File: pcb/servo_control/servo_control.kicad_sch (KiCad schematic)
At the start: 49 parts, among them J1 USB_B_Micro, J10 Conn_01x03_Female, J11 Conn_01x03_Female, J12 Conn_01x03_Female, J13 Conn_01x03_Female, J14 Conn_01x03_Female, J15 Conn_01x03_Female, J16 Conn_01x03_Female, J17 Conn_01x03_Female, J18 Conn_01x03_Female, J19 Conn_01x03_Female, J20 Conn_01x03_Female, J21 Conn_01x06_Male, J3 Conn_01x03_Female, J4 Conn_01x03_Female, J5 Conn_01x03_Female, J6 Conn_01x03_Female, J7 Conn_01x03_Female, J8 Conn_01x03_Female, J9 Conn_01x03_Female, SW1 ESP_PROG, SW2 ESP_RST, U1 PCA9685BS, U2 LM317_SOT-223, U3 ESP32-WROOM-32, U4 MPU-9250, U5 PCA9685BS

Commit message: finish pcb
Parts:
- removed D3: LED, LED_SMD:LED_0603_1608Metric, symbol Device:LED
- removed R5: 1K, Resistor_SMD:R_0603_1608Metric, symbol Device:R
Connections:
- net LED_1: now also U3.9 (IO33)
- net LED_2: now also U3.8 (IO32)
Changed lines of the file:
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@@
-    (stroke (width 0) (type default) (color 0 0 0 0))
-  )
-  (wire (pts (xy 284.48 45.72) (xy 289.56 45.72))
     (stroke (width 0) (type default) (color 0 0 0 0))
   )
@@
     (stroke (width 0) (type default) (color 0 0 0 0))
   )
-  (wire (pts (xy 297.18 45.72) (xy 302.26 45.72))
-    (stroke (width 0) (type default) (color 0 0 0 0))
-  )
   (wire (pts (xy 147.32 215.9) (xy 152.4 215.9))
     (stroke (width 0) (type default) (color 0 0 0 0))
@@
     (stroke (width 0) (type default) (color 0 0 0 0))
   )
-  (wire (pts (xy 309.88 45.72) (xy 317.5 45.72))
-    (stroke (width 0) (type default) (color 0 0 0 0))
-  )
   (polyline (pts (xy 15.24 278.13) (xy 120.65 278.13))
     (stroke (width 0) (type default) (color 0 0 0 0))
@@
     (stroke (width 0) (type default) (color 0 0 0 0))
   )
+  (wire (pts (xy 80.01 250.19) (xy 83.82 250.19))
+    (stroke (width 0) (type default) (color 0 0 0 0))
+  )
   (wire (pts (xy 165.1 215.9) (xy 170.18 215.9))
     (stroke (width 0) (type default) (color 0 0 0 0))
@@
     (stroke (width 0) (type default) (color 0 0 0 0))
   )
+  (wire (pts (xy 83.82 248.92) (xy 85.09 248.92))
+    (stroke (width 0) (type default) (color 0 0 0 0))
+  )
   (wire (pts (xy 373.38 91.44) (xy 377.19 91.44))
     (stroke (width 0) (type default) (color 0 0 0 0))
   )
-  (polyline (pts (xy 269.24 15.24) (xy 269.24 49.53))
+  (polyline (pts (xy 269.24 15.24) (xy 269.24 39.37))
     (stroke (width 0) (type default) (color 0 0 0 0))
   )
@@
     (stroke (width 0) (type default) (color 0 0 0 0))
   )
+  (wire (pts (xy 83.82 250.19) (xy 83.82 248.92))
+    (stroke (width 0) (type default) (color 0 0 0 0))
+  )
   (polyline (pts (xy 358.14 190.5) (xy 358.14 158.75))
     (stroke (width 0) (type default) (color 0 0 0 0))
@@
     (stroke (width 0) (type default) (color 0 0 0 0))
   )
+  (wire (pts (xy 80.01 252.73) (xy 85.09 252.73))
+    (stroke (width 0) (type default) (color 0 0 0 0))
+  )
   (polyline (pts (xy 90.17 113.03) (xy 90.17 71.12))
     (stroke (width 0) (type default) (color 0 0 0 0))
@@
     (stroke (width 0) (type default) (color 0 0 0 0))
   )
-  (polyline (pts (xy 326.39 49.53) (xy 326.39 15.24))
+  (polyline (pts (xy 326.39 39.37) (xy 326.39 15.24))
     (stroke (width 0) (type default) (color 0 0 0 0))
   )
@@
     (stroke (width 0) (type default) (color 0 0 0 0))
   )
-  (polyline (pts (xy 269.24 49.53) (xy 326.39 49.53))
+  (polyline (pts (xy 269.24 39.37) (xy 326.39 39.37))
     (stroke (width 0) (type default) (color 0 0 0 0))
   )
@@
     )
   )
+  (global_label "LED_2" (shape input) (at 85.09 248.92 0) (fields_autoplaced)
+    (effects (font (size 1.27 1.27)) (justify left))
+    (property "Intersheet References" "${INTERSHEET_REFS}" (id 0) (at 93.1274 248.8406 0)
+      (effects (font (size 1.27 1.27)) (justify left) hide)
+    )
+  )
   (global_label "VCC" (shape input) (at 370.84 207.01 180) (fields_autoplaced)
     (effects (font (size 1.27 1.27)) (justify right))
@@
     )
   )
-  (global_label "GND" (shape input) (at 317.5 45.72 0) (fields_autoplaced)
-    (effects (font (size 1.27 1.27)) (justify left))
-    (property "Intersheet References" "${INTERSHEET_REFS}" (id 0) (at 323.7836 45.6406 0)
-      (effects (font (size 1.27 1.27)) (justify left) hide)
-    )
-  )
   (global_label "PWM_0_13" (shape input) (at 370.84 179.07 180) (fields_autoplaced)
     (effects (font (size 1.27 1.27)) (justify right))
@@
     )
   )
+  (global_label "LED_1" (shape input) (at 85.09 252.73 0) (fields_autoplaced)
+    (effects (font (size 1.27 1.27)) (justify left))
+    (property "Intersheet References" "${INTERSHEET_REFS}" (id 0) (at 93.1274 252.6506 0)
+      (effects (font (size 1.27 1.27)) (justify left) hide)
+    )
+  )
   (global_label "FTDI_CTS" (shape input) (at 73.66 54.61 0) (fields_autoplaced)
     (effects (font (size 1.27 1.27)) (justify left))
@@
     (property "Intersheet References" "${INTERSHEET_REFS}" (id 0) (at 160.7398 65.9606 0)
       (effects (font (size 1.27 1.27)) (justify left) hide)
-    )
-  )
-  (global_label "LED_3" (shape input) (at 284.48 45.72 180) (fields_autoplaced)
-    (effects (font (size 1.27 1.27)) (justify right))
-    (property "Intersheet References" "${INTERSHEET_REFS}" (id 0) (at 276.4426 45.6406 0)
-      (effects (font (size 1.27 1.27)) (justify right) hide)
     )
   )
@@
     )
     (property "Datasheet" "~" (id 3) (at 27.94 204.47 0)
-      (effects (font (size 1.27 1.27)) hide)
-    )
-    (pin "1")
-    (pin "2")
-  )
-  (symbol (lib_id "Device:R") (at 293.37 45.72 90) (unit 1)
-    (in_bom yes) (on_board yes) (fields_autoplaced)
-    (property "Reference" "R5" (id 0) (at 293.37 39.37 90))
-    (property "Value" "1K" (id 1) (at 293.37 41.91 90))
-    (property "Footprint" "Resistor_SMD:R_0603_1608Metric" (id 2) (at 293.37 47.498 90)
-      (effects (font (size 1.27 1.27)) hide)
-    )
-    (property "Datasheet" "~" (id 3) (at 293.37 45.72 0)
-      (effects (font (size 1.27 1.27)) hide)
-    )
-    (pin "1")
-    (pin "2")
-  )
-  (symbol (lib_id "Device:LED") (at 306.07 45.72 180) (unit 1)
-    (in_bom yes) (on_board yes)
-    (property "Reference" "D3" (id 0) (at 306.07 41.91 0))
-    (property "Value" "LED" (id 1) (at 306.07 39.37 0))
-    (property "Footprint" "LED_SMD:LED_0603_1608Metric" (id 2) (at 306.07 45.72 0)
-      (effects (font (size 1.27 1.27)) hide)
-    )
-    (property "Datasheet" "~" (id 3) (at 306.07 45.72 0)
       (effects (font (size 1.27 1.27)) hide)
     )
@@
       (reference "D2") (unit 1) (value "LED") (footprint "LED_SMD:LED_0603_1608Metric")
     )
-    (path "/0e3cf2b7-1e28-4d8a-863a-31ad64beb94b"
-      (reference "D3") (unit 1) (value "LED") (footprint "LED_SMD:LED_0603_1608Metric")
-    )
     (path "/9c8a2cf4-c30a-426a-b3e9-2e2ded2f331a"
       (reference "J1") (unit 1) (value "USB_B_Micro") (footprint "Connector_USB:USB_Micro-B_Molex-105017-0001")
@@
       (reference "R4") (unit 1) (value "1K") (footprint "Resistor_SMD:R_0603_1608Metric")
     )
-    (path "/0e2c80ab-b30b-4b41-93fc-dc4b3b81fc4c"
-      (reference "R5") (unit 1) (value "1K") (footprint "Resistor_SMD:R_0603_1608Metric")
-    )
     (path "/6f2988a4-b516-472d-b2a2-6928c828e26c"

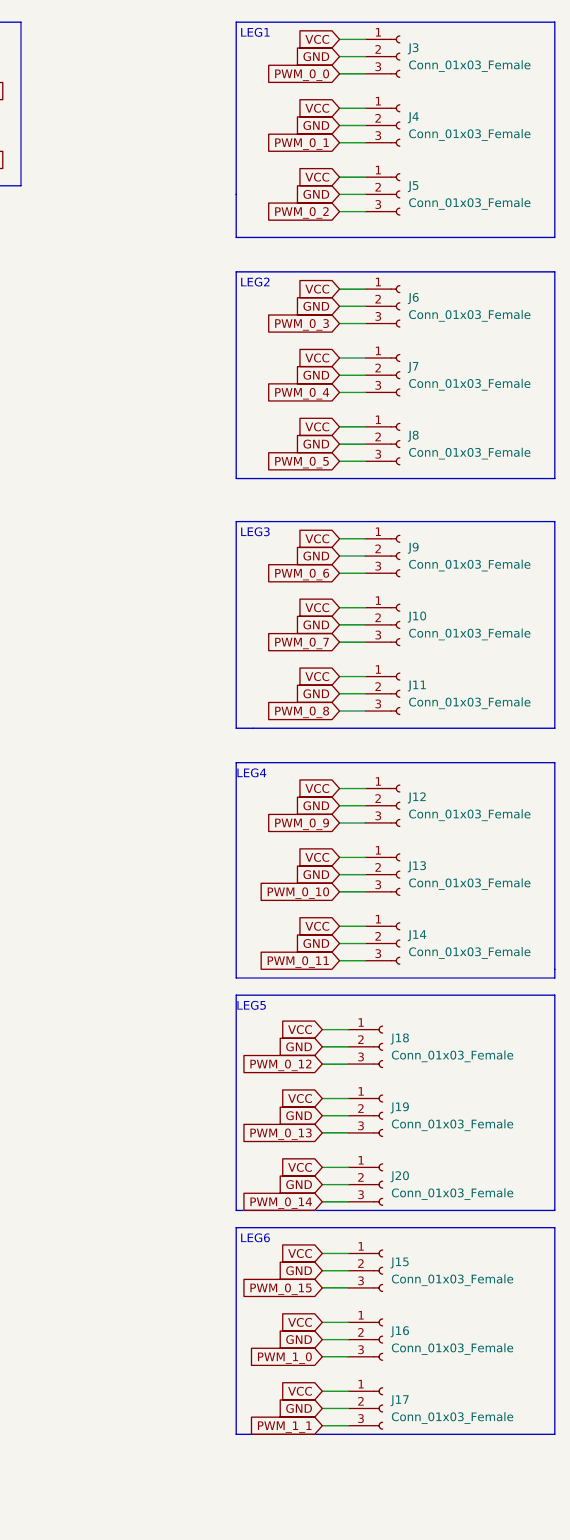
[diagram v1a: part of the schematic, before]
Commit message: fix servo header
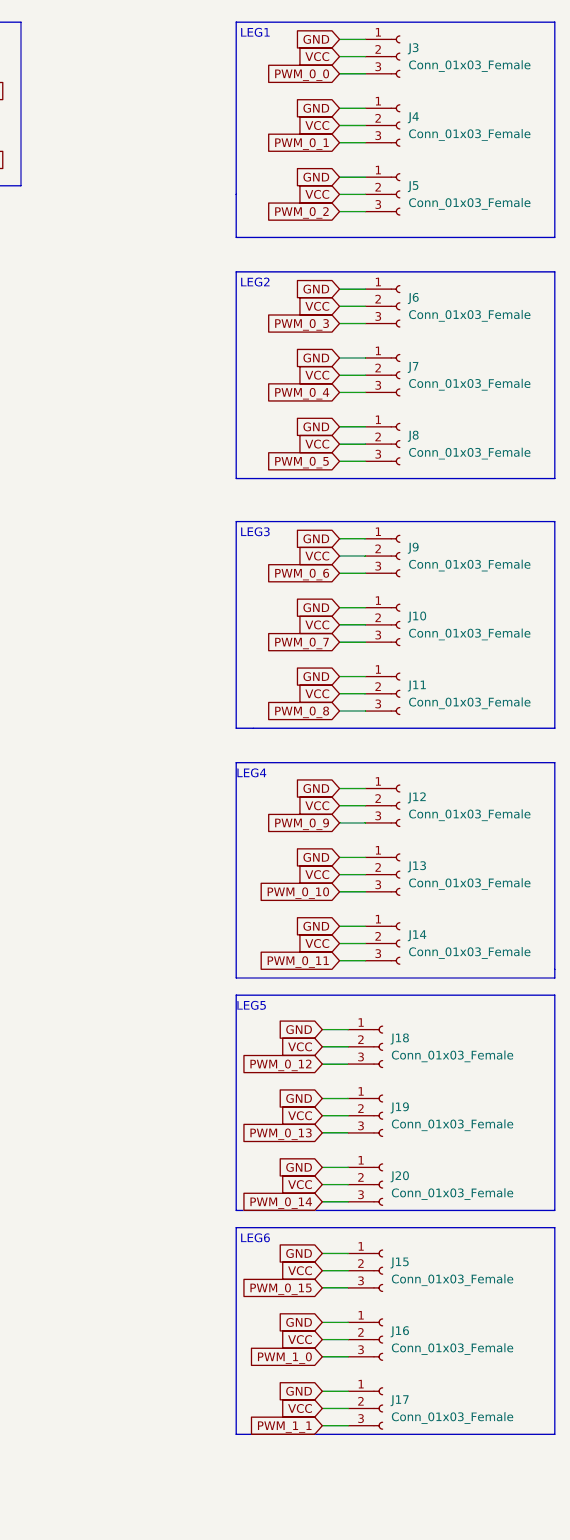
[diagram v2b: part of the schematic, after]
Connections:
- net GND: now also J10.1 (Pin_1), J11.1 (Pin_1), J12.1 (Pin_1), J13.1 (Pin_1), J14.1 (Pin_1), J15.1 (Pin_1), J16.1 (Pin_1), J17.1 (Pin_1), J18.1 (Pin_1), J19.1 (Pin_1), J20.1 (Pin_1), J3.1 (Pin_1), J4.1 (Pin_1), J5.1 (Pin_1), J6.1 (Pin_1), J7.1 (Pin_1), J8.1 (Pin_1), J9.1 (Pin_1); no longer J10.2 (Pin_2), J11.2 (Pin_2), J12.2 (Pin_2), J13.2 (Pin_2), J14.2 (Pin_2), J15.2 (Pin_2), J16.2 (Pin_2), J17.2 (Pin_2), J18.2 (Pin_2), J19.2 (Pin_2), J20.2 (Pin_2), J3.2 (Pin_2), J4.2 (Pin_2), J5.2 (Pin_2), J6.2 (Pin_2), J7.2 (Pin_2), J8.2 (Pin_2), J9.2 (Pin_2)
- net VCC: now also J10.2 (Pin_2), J11.2 (Pin_2), J12.2 (Pin_2), J13.2 (Pin_2), J14.2 (Pin_2), J15.2 (Pin_2), J16.2 (Pin_2), J17.2 (Pin_2), J18.2 (Pin_2), J19.2 (Pin_2), J20.2 (Pin_2), J3.2 (Pin_2), J4.2 (Pin_2), J5.2 (Pin_2), J6.2 (Pin_2), J7.2 (Pin_2), J8.2 (Pin_2), J9.2 (Pin_2); no longer J10.1 (Pin_1), J11.1 (Pin_1), J12.1 (Pin_1), J13.1 (Pin_1), J14.1 (Pin_1), J15.1 (Pin_1), J16.1 (Pin_1), J17.1 (Pin_1), J18.1 (Pin_1), J19.1 (Pin_1), J20.1 (Pin_1), J3.1 (Pin_1), J4.1 (Pin_1), J5.1 (Pin_1), J6.1 (Pin_1), J7.1 (Pin_1), J8.1 (Pin_1), J9.1 (Pin_1)

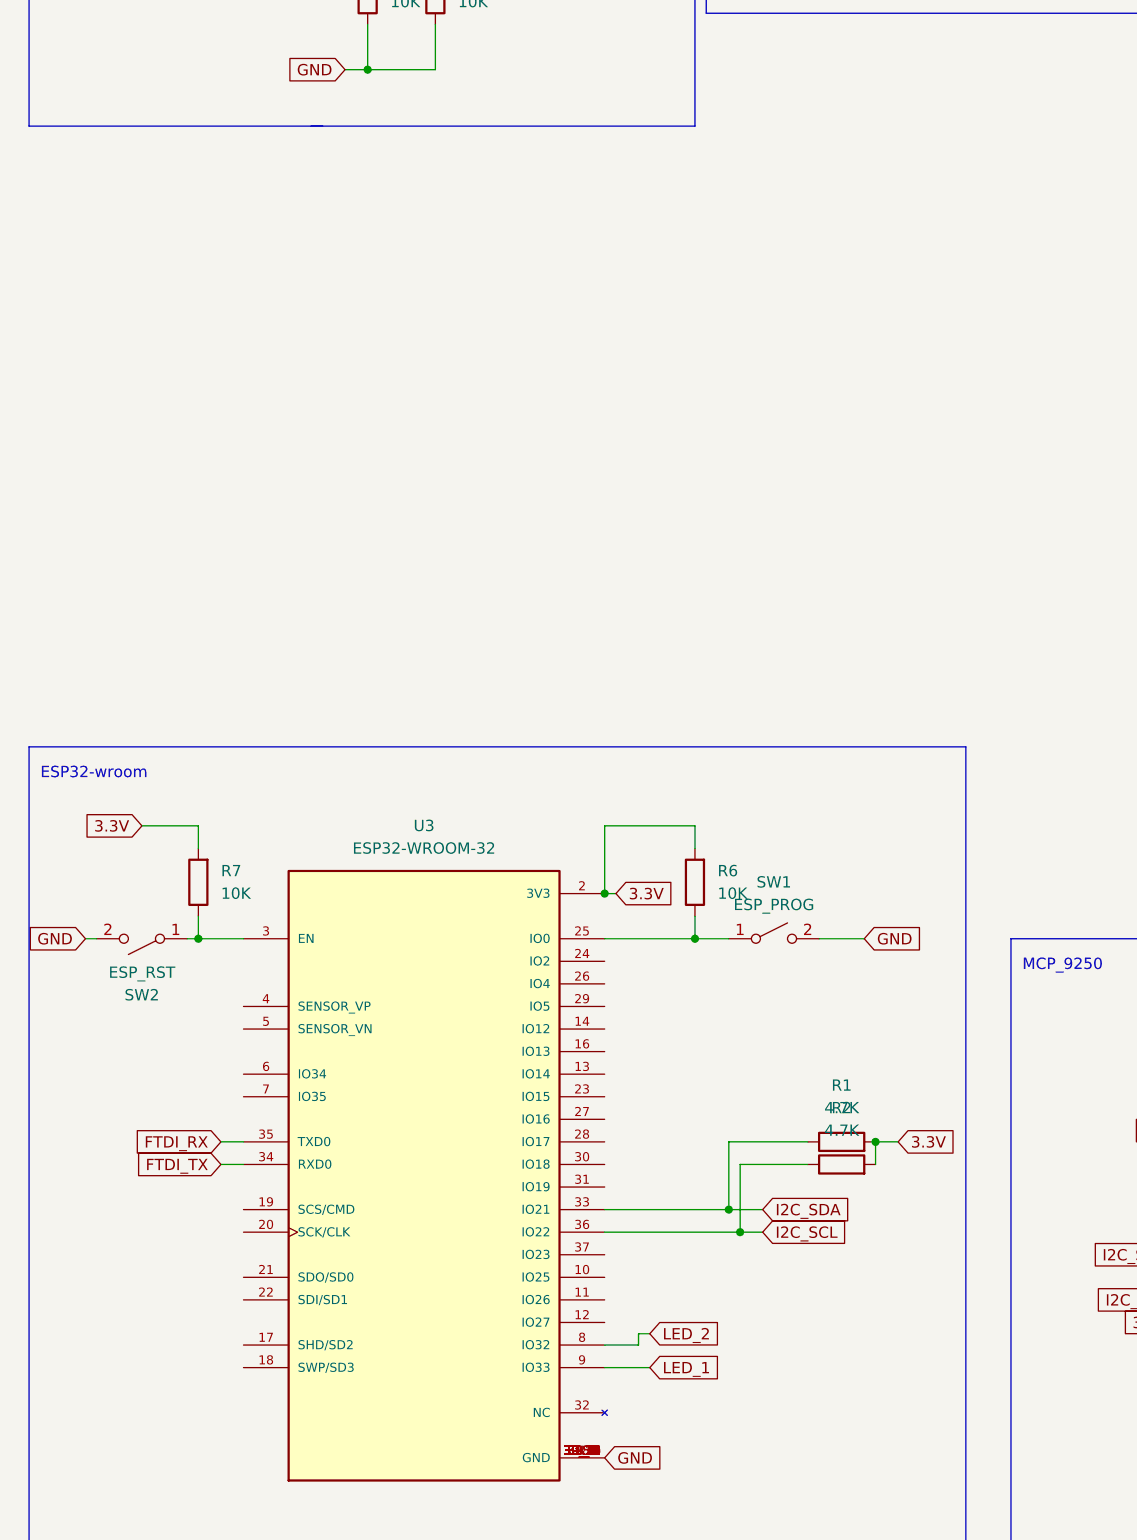
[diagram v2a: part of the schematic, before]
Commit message: edit project name
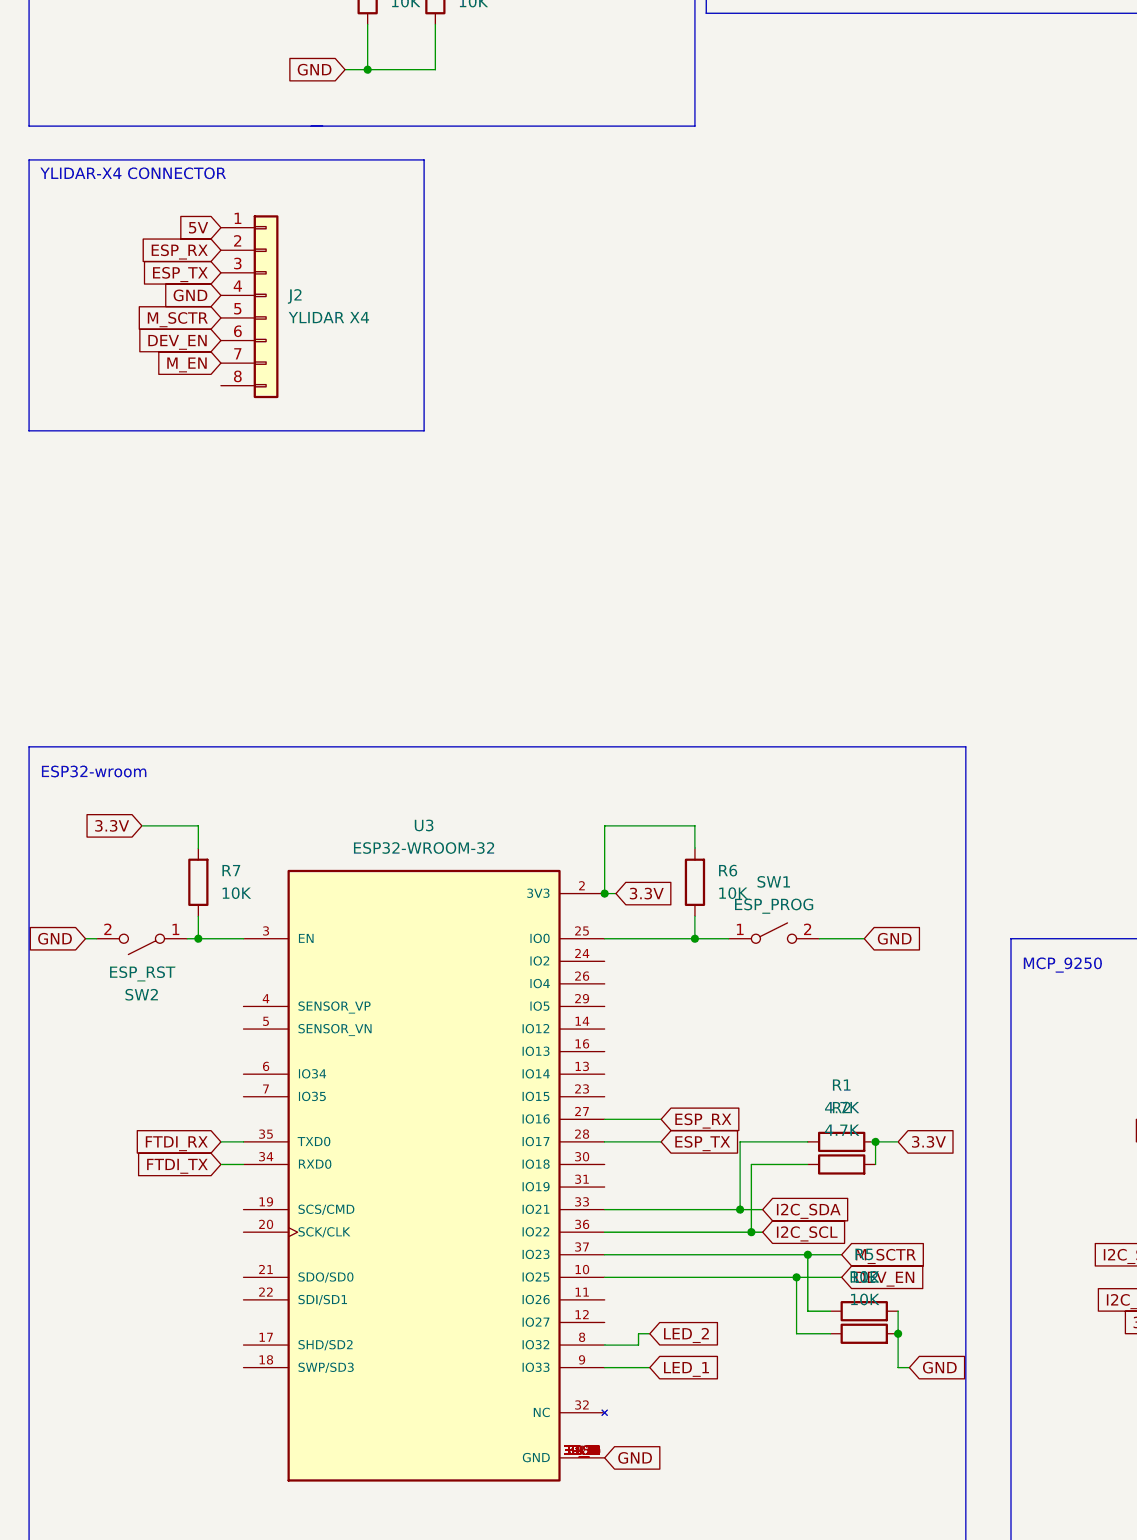
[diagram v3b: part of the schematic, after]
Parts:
- added J2: YLIDAR X4, Connector_Hirose:Hirose_DF13-08P-1.25DSA_1x08_P1.25mm_Vertical, symbol Connector_Generic:Conn_01x08
- added R12, R5: 10K, Resistor_SMD:R_0603_1608Metric, symbol Device:R
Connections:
- net GND: now also J2.4 (Pin_4), R12.2, R5.2
- net DEV_EN: now reaches U3.10 (IO25)
- net DEV_EN: now also J2.6 (Pin_6), R12.1
- net ESP_RX: now reaches U3.27 (IO16)
- net ESP_RX: now also J2.2 (Pin_2)
- net ESP_TX: now reaches U3.28 (IO17)
- net ESP_TX: now also J2.3 (Pin_3)
- net M_SCTR: now reaches U3.37 (IO23)
- net M_SCTR: now also J2.5 (Pin_5), R5.1
- new net 5V: J2.1 (Pin_1)
- new net M_EN: J2.7 (Pin_7)
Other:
- note added: "YLIDAR-X4 CONNECTOR"
